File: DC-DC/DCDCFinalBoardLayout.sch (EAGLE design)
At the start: 39 parts, among them J1 1200845133, J2 1200845133, K1 ALZ12B12W

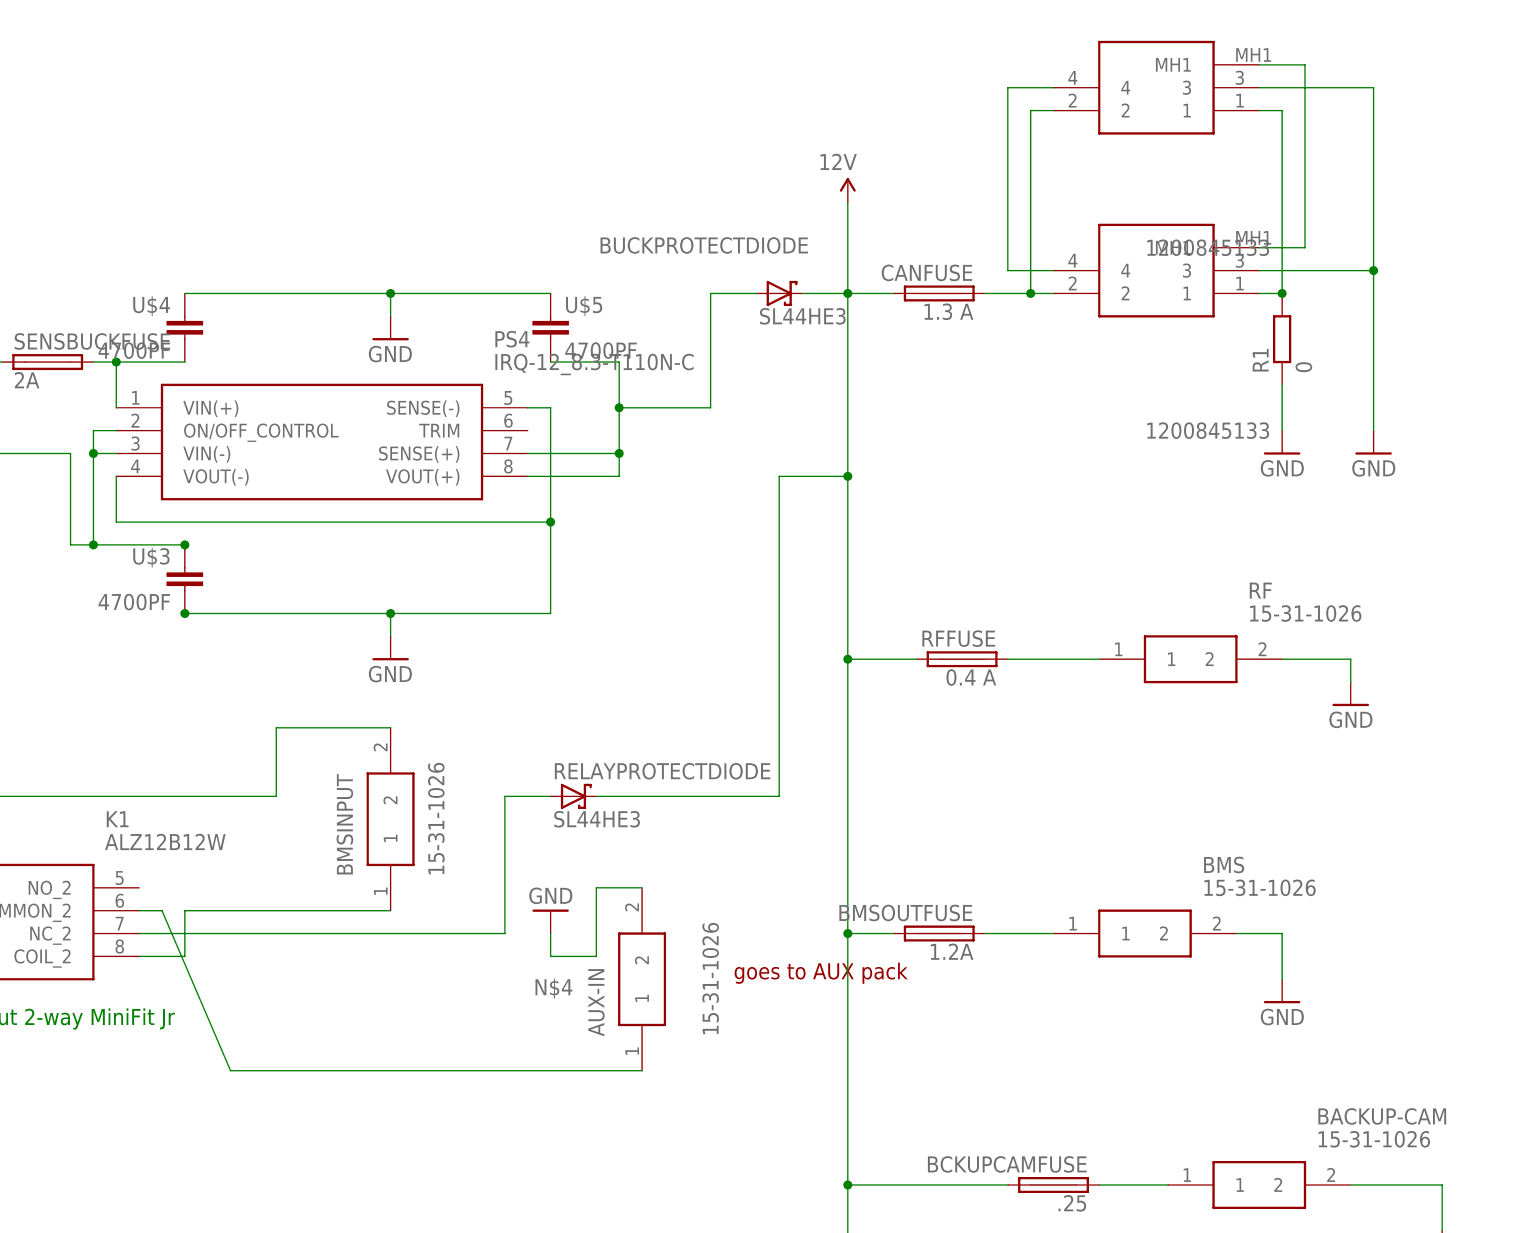
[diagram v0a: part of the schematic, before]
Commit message: DCDC Final Board Layout & Schematic
The final iteration of a lengthy design process, involving input from a variety of parties, with specializations ranging from physics, to electrical engineering, to electrical engineering, to electrical engineering. Peace and Love :100:
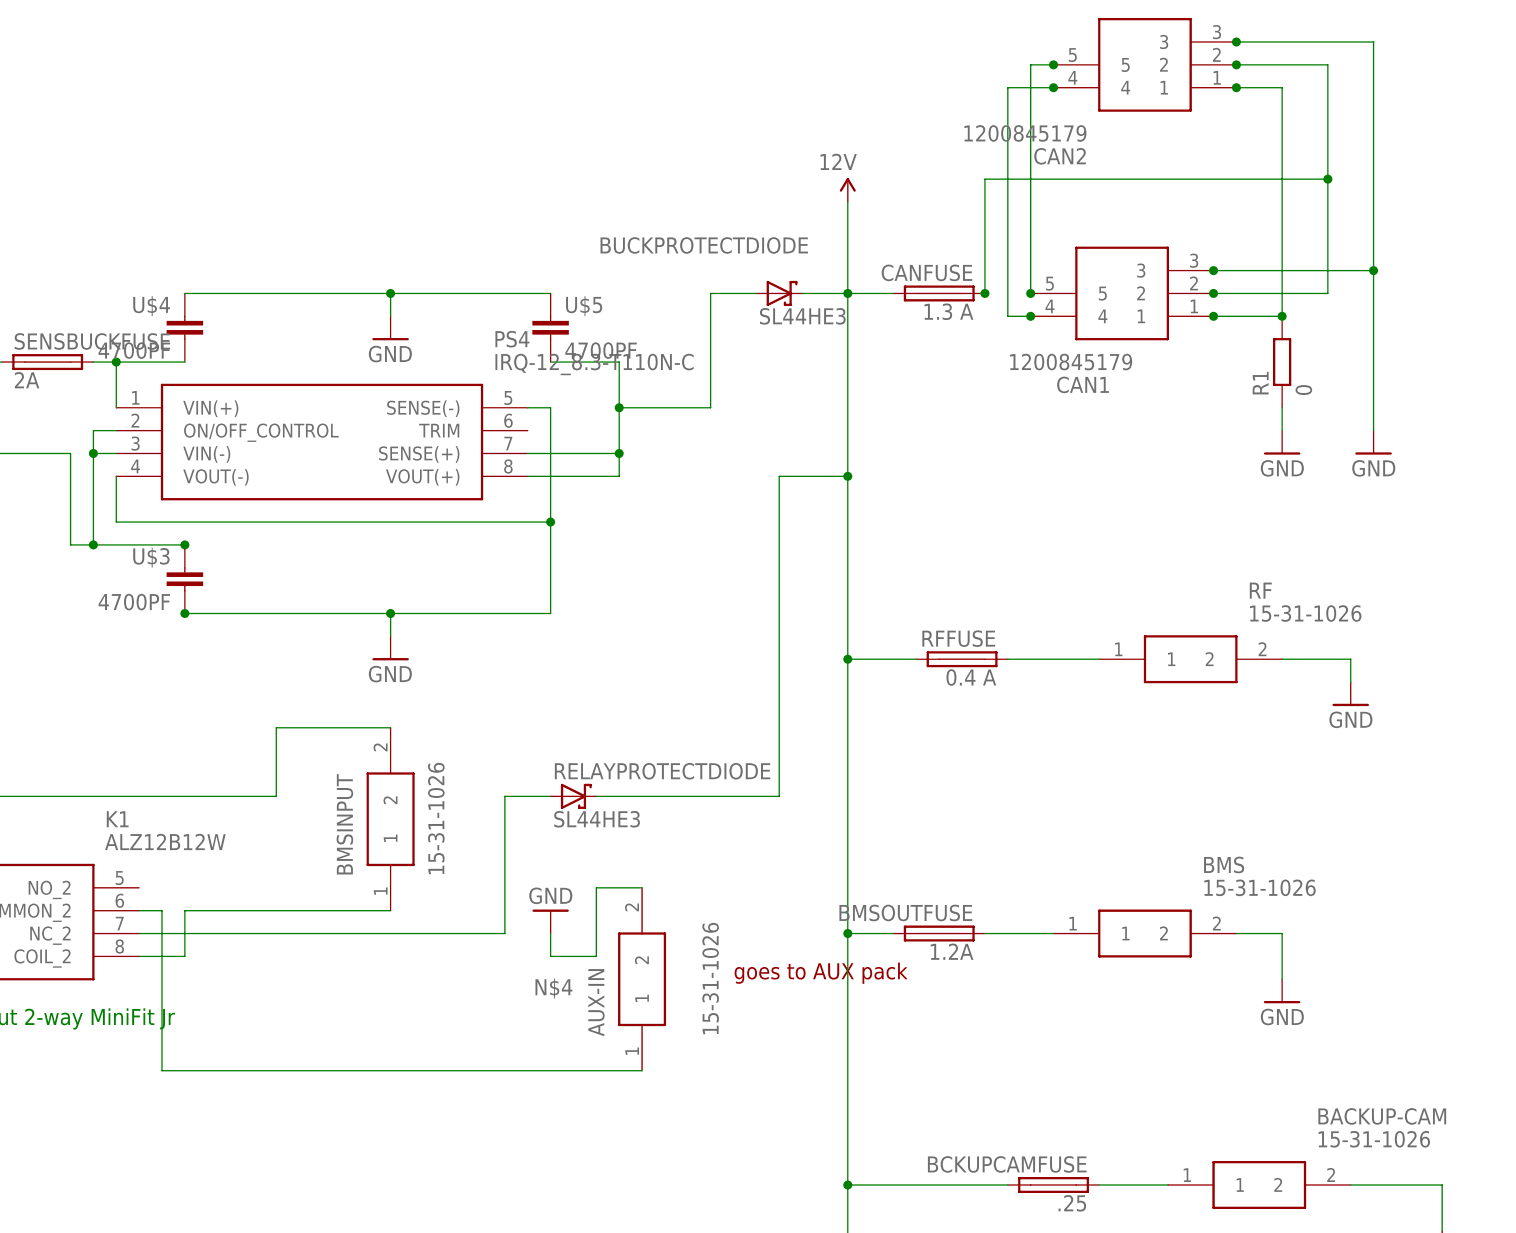
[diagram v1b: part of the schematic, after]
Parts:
- removed J1, J2: 1200845133, SamacSys_Parts:1200845133
- added CAN1, CAN2: 1200845179, SamacSys_Parts:1200845179
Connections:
- removed net N$16: CANFUSE.1, J1.2, J2.2
- new net N$19: CAN1.5, CAN2.5
- net GND: now also CAN1.3, CAN2.3; no longer J1.3, J2.3
- net N$17: now also CAN1.1, CAN2.1; no longer J1.1, J2.1
- net N$18: now also CAN1.4, CAN2.4; no longer J1.4, J2.4
- net N$20: now also CAN1.2, CAN2.2, CANFUSE.1; no longer J1.MH1, J2.MH1
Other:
- moved on the sheet: R1
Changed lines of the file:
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@@
 <part name="AUX-IN" library="SamacSys_Parts" deviceset="15-31-1026" device=""/>
 <part name="BMSINPUT" library="SamacSys_Parts" deviceset="15-31-1026" device=""/>
-<part name="J1" library="SamacSys_Parts" deviceset="1200845133" device=""/>
 <part name="VARBUCKPROTECTDIODE" library="diode" deviceset="SL44HE3" device=""/>
 <part name="R1" library="eagle-ltspice" library_urn="urn:adsk.eagle:library:217" deviceset="R" device="" package3d_urn="urn:adsk.eagle:package:13300/1" value="0"/>
 <part name="GND17" library="SparkFun-Aesthetics" deviceset="GND" device=""/>
-<part name="J2" library="SamacSys_Parts" deviceset="1200845133" device=""/>
+<part name="CAN1" library="SamacSys_Parts" deviceset="1200845179" device=""/>
+<part name="CAN2" library="SamacSys_Parts" deviceset="1200845179" device=""/>
 </parts>
 <sheets>
@@
 <attribute name="VALUE" x="-208.28" y="72.39" size="1.778" layer="96" rot="R90" align="center-left"/>
 </instance>
-<instance part="J1" gate="G$1" x="-116.84" y="137.16" smashed="yes" rot="R180">
-<attribute name="VALUE" x="-115.57" y="121.92" size="1.778" layer="96" rot="R180" align="center-left"/>
-</instance>
 <instance part="VARBUCKPROTECTDIODE" gate="SL44HE3" x="-190.5" y="-40.64" smashed="yes">
 <attribute name="NAME" x="-210.566" y="-36.195" size="1.778" layer="95"/>
 <attribute name="VALUE" x="-192.786" y="-44.069" size="1.778" layer="96"/>
 </instance>
-<instance part="R1" gate="G$1" x="-114.3" y="132.08" smashed="yes" rot="R90">
-<attribute name="NAME" x="-115.7986" y="128.27" size="1.778" layer="95" rot="R90"/>
-<attribute name="VALUE" x="-110.998" y="128.27" size="1.778" layer="96" rot="R90"/>
+<instance part="R1" gate="G$1" x="-114.3" y="129.54" smashed="yes" rot="R90">
+<attribute name="NAME" x="-115.7986" y="125.73" size="1.778" layer="95" rot="R90"/>
+<attribute name="VALUE" x="-110.998" y="125.73" size="1.778" layer="96" rot="R90"/>
 </instance>
 <instance part="GND17" gate="1" x="-114.3" y="119.38" smashed="yes" rot="MR0">
 <attribute name="VALUE" x="-111.76" y="116.84" size="1.778" layer="96" rot="MR0"/>
 </instance>
-<instance part="J2" gate="G$1" x="-116.84" y="157.48" smashed="yes" rot="R180">
-<attribute name="VALUE" x="-115.57" y="142.24" size="1.778" layer="96" rot="R180" align="center-left"/>
+<instance part="CAN1" gate="G$1" x="-121.92" y="134.62" smashed="yes" rot="R180">
+<attribute name="NAME" x="-133.35" y="127" size="1.778" layer="95" rot="R180" align="center-left"/>
+<attribute name="VALUE" x="-130.81" y="129.54" size="1.778" layer="96" rot="R180" align="center-left"/>
+</instance>
+<instance part="CAN2" gate="G$1" x="-119.38" y="160.02" smashed="yes" rot="R180">
+<attribute name="NAME" x="-135.89" y="152.4" size="1.778" layer="95" rot="R180" align="center-left"/>
+<attribute name="VALUE" x="-135.89" y="154.94" size="1.778" layer="96" rot="R180" align="center-left"/>
 </instance>
 </instances>
@@
 </segment>
 <segment>
-<pinref part="J1" gate="G$1" pin="3"/>
 <pinref part="GND9" gate="1" pin="GND"/>
-<wire x1="-116.84" y1="139.7" x2="-104.14" y2="139.7" width="0.1524" layer="91"/>
+<wire x1="-121.92" y1="139.7" x2="-104.14" y2="139.7" width="0.1524" layer="91"/>
 <wire x1="-104.14" y1="139.7" x2="-104.14" y2="121.92" width="0.1524" layer="91"/>
-<pinref part="J2" gate="G$1" pin="3"/>
-<wire x1="-116.84" y1="160.02" x2="-104.14" y2="160.02" width="0.1524" layer="91"/>
-<wire x1="-104.14" y1="160.02" x2="-104.14" y2="139.7" width="0.1524" layer="91"/>
+<wire x1="-104.14" y1="165.1" x2="-104.14" y2="139.7" width="0.1524" layer="91"/>
 <junction x="-104.14" y="139.7"/>
+<pinref part="CAN1" gate="G$1" pin="3"/>
+<pinref part="CAN2" gate="G$1" pin="3"/>
+<wire x1="-104.14" y1="165.1" x2="-119.38" y2="165.1" width="0.1524" layer="91"/>
+<junction x="-119.38" y="165.1"/>
+<junction x="-121.92" y="139.7"/>
 </segment>
 <segment>
 <pinref part="GND17" gate="1" pin="GND"/>
 <pinref part="R1" gate="G$1" pin="1"/>
-<wire x1="-114.3" y1="121.92" x2="-114.3" y2="127" width="0.1524" layer="91"/>
+<wire x1="-114.3" y1="124.46" x2="-114.3" y2="121.92" width="0.1524" layer="91"/>
 </segment>
 </net>
@@
 <net name="N$2" class="0">
 <segment>
-<wire x1="-185.42" y1="50.8" x2="-231.14" y2="50.8" width="0.1524" layer="91"/>
-<wire x1="-231.14" y1="50.8" x2="-238.76" y2="68.58" width="0.1524" layer="91"/>
+<wire x1="-185.42" y1="50.8" x2="-238.76" y2="50.8" width="0.1524" layer="91"/>
+<wire x1="-238.76" y1="50.8" x2="-238.76" y2="68.58" width="0.1524" layer="91"/>
 <pinref part="K1" gate="G$1" pin="COMMON_2"/>
 <wire x1="-238.76" y1="68.58" x2="-241.3" y2="68.58" width="0.1524" layer="91"/>
@@
 </segment>
 </net>
-<net name="N$16" class="0">
-<segment>
+<net name="N$17" class="0">
+<segment>
+<pinref part="R1" gate="G$1" pin="2"/>
+<wire x1="-114.3" y1="160.02" x2="-114.3" y2="134.62" width="0.1524" layer="91"/>
+<pinref part="CAN1" gate="G$1" pin="1"/>
+<wire x1="-121.92" y1="134.62" x2="-114.3" y2="134.62" width="0.1524" layer="91"/>
+<junction x="-114.3" y="134.62"/>
+<pinref part="CAN2" gate="G$1" pin="1"/>
+<wire x1="-114.3" y1="160.02" x2="-119.38" y2="160.02" width="0.1524" layer="91"/>
+<junction x="-119.38" y="160.02"/>
+<junction x="-121.92" y="134.62"/>
+</segment>
+</net>
+<net name="N$18" class="0">
+<segment>
+<wire x1="-139.7" y1="160.02" x2="-144.78" y2="160.02" width="0.1524" layer="91"/>
+<wire x1="-144.78" y1="160.02" x2="-144.78" y2="134.62" width="0.1524" layer="91"/>
+<pinref part="CAN1" gate="G$1" pin="4"/>
+<wire x1="-144.78" y1="134.62" x2="-142.24" y2="134.62" width="0.1524" layer="91"/>
+<pinref part="CAN2" gate="G$1" pin="4"/>
+<junction x="-142.24" y="134.62"/>
+<junction x="-139.7" y="160.02"/>
+</segment>
+</net>
+<net name="N$20" class="0">
+<segment>
+<wire x1="-109.22" y1="162.56" x2="-119.38" y2="162.56" width="0.1524" layer="91"/>
+<pinref part="CAN2" gate="G$1" pin="2"/>
 <pinref part="CANFUSE" gate="F1" pin="1"/>
-<pinref part="J1" gate="G$1" pin="2"/>
-<wire x1="-147.32" y1="137.16" x2="-142.24" y2="137.16" width="0.1524" layer="91"/>
-<pinref part="J2" gate="G$1" pin="2"/>
-<wire x1="-142.24" y1="137.16" x2="-139.7" y2="137.16" width="0.1524" layer="91"/>
-<wire x1="-139.7" y1="157.48" x2="-142.24" y2="157.48" width="0.1524" layer="91"/>
-<wire x1="-142.24" y1="157.48" x2="-142.24" y2="137.16" width="0.1524" layer="91"/>
+<wire x1="-147.32" y1="137.16" x2="-147.32" y2="149.86" width="0.1524" layer="91"/>
+<wire x1="-147.32" y1="149.86" x2="-109.22" y2="149.86" width="0.1524" layer="91"/>
+<wire x1="-109.22" y1="149.86" x2="-109.22" y2="137.16" width="0.1524" layer="91"/>
+<pinref part="CAN1" gate="G$1" pin="2"/>
+<wire x1="-109.22" y1="137.16" x2="-121.92" y2="137.16" width="0.1524" layer="91"/>
+<wire x1="-109.22" y1="162.56" x2="-109.22" y2="149.86" width="0.1524" layer="91"/>
+<junction x="-109.22" y="149.86"/>
+<junction x="-147.32" y="137.16"/>
+<junction x="-119.38" y="162.56"/>
+<junction x="-121.92" y="137.16"/>
+</segment>
+</net>
+<net name="N$19" class="0">
+<segment>
+<pinref part="CAN1" gate="G$1" pin="5"/>
+<pinref part="CAN2" gate="G$1" pin="5"/>
+<wire x1="-142.24" y1="137.16" x2="-142.24" y2="162.56" width="0.1524" layer="91"/>
+<wire x1="-142.24" y1="162.56" x2="-139.7" y2="162.56" width="0.1524" layer="91"/>
 <junction x="-142.24" y="137.16"/>
-</segment>
-</net>
-<net name="N$17" class="0">
-<segment>
-<pinref part="R1" gate="G$1" pin="2"/>
-<pinref part="J1" gate="G$1" pin="1"/>
-<wire x1="-114.3" y1="137.16" x2="-116.84" y2="137.16" width="0.1524" layer="91"/>
-<pinref part="J2" gate="G$1" pin="1"/>
-<wire x1="-116.84" y1="157.48" x2="-114.3" y2="157.48" width="0.1524" layer="91"/>
-<wire x1="-114.3" y1="157.48" x2="-114.3" y2="137.16" width="0.1524" layer="91"/>
-<junction x="-114.3" y="137.16"/>
-</segment>
-</net>
-<net name="N$18" class="0">
-<segment>
-<pinref part="J2" gate="G$1" pin="4"/>
-<wire x1="-139.7" y1="160.02" x2="-144.78" y2="160.02" width="0.1524" layer="91"/>
-<wire x1="-144.78" y1="160.02" x2="-144.78" y2="139.7" width="0.1524" layer="91"/>
-<pinref part="J1" gate="G$1" pin="4"/>
-<wire x1="-144.78" y1="139.7" x2="-139.7" y2="139.7" width="0.1524" layer="91"/>
-</segment>
-</net>
-<net name="N$20" class="0">
-<segment>
-<pinref part="J1" gate="G$1" pin="MH1"/>
-<wire x1="-116.84" y1="142.24" x2="-111.76" y2="142.24" width="0.1524" layer="91"/>
-<wire x1="-111.76" y1="142.24" x2="-111.76" y2="162.56" width="0.1524" layer="91"/>
-<pinref part="J2" gate="G$1" pin="MH1"/>
-<wire x1="-111.76" y1="162.56" x2="-116.84" y2="162.56" width="0.1524" layer="91"/>
-</segment>
-</net>
+<junction x="-139.7" y="162.56"/>
+</segment>
+</net>

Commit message: updated gerber files with new diode
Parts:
- removed BUCKPROTECTDIODE, RELAYPROTECTDIODE, VARBUCKPROTECTDIODE: SL44HE3, diode:SL44HE3
- added Q1, Q2: BUZ10, transistor-fet:BUZ10
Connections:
- net 12V: now also Q1.D, Q2.D; no longer BUCKPROTECTDIODE.C, RELAYPROTECTDIODE.C, VARBUCKPROTECTDIODE.C
- net N$13: now also Q1.G; no longer VARBUCKPROTECTDIODE.A
- net N$15: now also Q2.G; no longer BUCKPROTECTDIODE.A
- net N$4: now also Q2.S; no longer RELAYPROTECTDIODE.A
